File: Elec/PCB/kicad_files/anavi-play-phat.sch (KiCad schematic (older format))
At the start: 8 parts

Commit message: Il faut refaire le pcb avec le port usb de l'autre coté
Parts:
- SW_BCK1, SW_DWN1, SW_L1, SW_OK1, SW_R1, SW_UP1: footprint (none) -> boutton:boutton__5mx5m
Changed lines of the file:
@@
 EESchema Schematic File Version 4
-LIBS:anavi-play-phat-cache
 EELAYER 30 0
 EELAYER END
@@
 F 0 "SW_DWN1" H 7025 3973 50  0000 C CNN
 F 1 "boutton_5mx5m" H 7025 3974 50  0001 C CNN
-F 2 "" H 7150 3700 50  0001 C CNN
+F 2 "boutton:boutton__5mx5m" H 7150 3700 50  0001 C CNN
 F 3 "" H 7150 3700 50  0001 C CNN
 	1    7150 3800
@@
 F 0 "SW_UP1" H 7025 4323 50  0000 C CNN
 F 1 "boutton_5mx5" H 7025 4324 50  0001 C CNN
-F 2 "" H 7150 4050 50  0001 C CNN
+F 2 "boutton:boutton__5mx5m" H 7150 4050 50  0001 C CNN
 F 3 "" H 7150 4050 50  0001 C CNN
 	1    7150 4150
@@
 F 0 "SW_L1" H 7025 4723 50  0000 C CNN
 F 1 "boutton_5mx5m" H 7025 4724 50  0001 C CNN
-F 2 "" H 7150 4450 50  0001 C CNN
+F 2 "boutton:boutton__5mx5m" H 7150 4450 50  0001 C CNN
 F 3 "" H 7150 4450 50  0001 C CNN
 	1    7150 4550
@@
 F 0 "SW_R1" H 7025 5073 50  0000 C CNN
 F 1 "boutton_5mx5m" H 7025 5074 50  0001 C CNN
-F 2 "" H 7150 4800 50  0001 C CNN
+F 2 "boutton:boutton__5mx5m" H 7150 4800 50  0001 C CNN
 F 3 "" H 7150 4800 50  0001 C CNN
 	1    7150 4900
@@
 F 0 "SW_OK1" H 7025 5473 50  0000 C CNN
 F 1 "boutton_5mx5m" H 7025 5474 50  0001 C CNN
-F 2 "" H 7150 5200 50  0001 C CNN
+F 2 "boutton:boutton__5mx5m" H 7150 5200 50  0001 C CNN
 F 3 "" H 7150 5200 50  0001 C CNN
 	1    7150 5300
@@
 F 0 "SW_BCK1" H 7025 5823 50  0000 C CNN
 F 1 "boutton_5mx5m" H 7025 5824 50  0001 C CNN
-F 2 "" H 7150 5550 50  0001 C CNN
+F 2 "boutton:boutton__5mx5m" H 7150 5550 50  0001 C CNN
 F 3 "" H 7150 5550 50  0001 C CNN
 	1    7150 5650

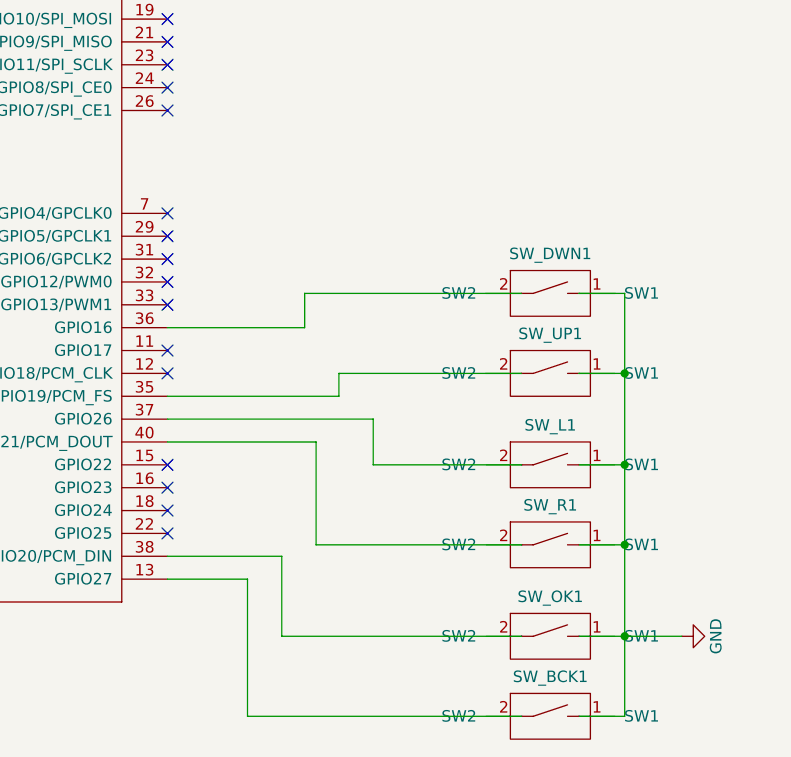
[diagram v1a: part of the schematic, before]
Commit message: PCB v3 correction USB
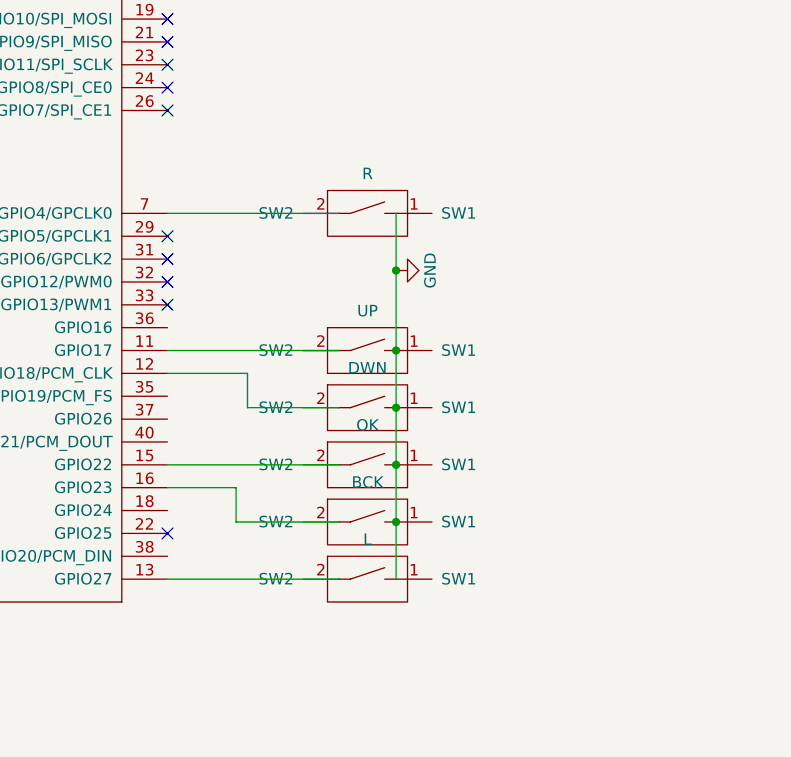
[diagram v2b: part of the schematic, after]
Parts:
- removed SW_BCK1, SW_DWN1, SW_L1, SW_OK1, SW_R1: boutton_5mx5m, boutton:boutton__5mx5m, symbol boutton:boutton_5mx5m
- removed SW_UP1: boutton_5mx5, boutton:boutton__5mx5m, symbol boutton:boutton_5mx5m
- added BCK, DWN, L, OK, R, UP: boutton_6mx6m, boutton:boutton__6mx6m, symbol boutton:boutton_6mx6m
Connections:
- net GND: now also BCK.1 (SW1), DWN.1 (SW1), L.1 (SW1), OK.1 (SW1), R.1 (SW1), UP.1 (SW1)
- net at RASP_CONN1.11 (GPIO17): now also UP.2 (SW2)
- net at RASP_CONN1.12 (GPIO18/PCM_CLK): now also DWN.2 (SW2)
- net at RASP_CONN1.13 (GPIO27): now also L.2 (SW2)
- net at RASP_CONN1.15 (GPIO22): now also OK.2 (SW2)
- net at RASP_CONN1.16 (GPIO23): now also BCK.2 (SW2)
- net at RASP_CONN1.7 (GPIO4/GPCLK0): now also R.2 (SW2)
- no-connect marks 20 -> 14
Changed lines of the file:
@@
 $EndComp
 NoConn ~ 5350 4850
-NoConn ~ 5350 4750
-NoConn ~ 5350 4650
 NoConn ~ 5350 3750
 NoConn ~ 5350 2900
 NoConn ~ 5350 3000
-NoConn ~ 5350 4150
 NoConn ~ 5350 3850
 NoConn ~ 5350 2600
@@
 L anavi-play-phat-rescue:GND-power #PWR016
 U 1 1 5B2D1552
-P 7600 5300
-F 0 "#PWR016" H 7600 5050 50  0001 C CNN
-F 1 "GND" H 7600 5150 50  0000 C CNN
-F 2 "" H 7600 5300 50  0001 C CNN
-F 3 "" H 7600 5300 50  0001 C CNN
-	1    7600 5300
+P 6350 3700
+F 0 "#PWR016" H 6350 3450 50  0001 C CNN
+F 1 "GND" H 6350 3550 50  0000 C CNN
+F 2 "" H 6350 3700 50  0001 C CNN
+F 3 "" H 6350 3700 50  0001 C CNN
+	1    6350 3700
 	0    -1   -1   0
 $EndComp
@@
 	1    0    0    -1
 $EndComp
-Wire Wire Line
-	5350 3950 5950 3950
-Wire Wire Line
-	5950 3950 5950 3800
-Wire Wire Line
-	5950 3800 6900 3800
-Wire Wire Line
-	5350 4250 6100 4250
-Wire Wire Line
-	6100 4250 6100 4150
-Wire Wire Line
-	6100 4150 6900 4150
-Wire Wire Line
-	5350 4950 5850 4950
-Wire Wire Line
-	5850 4950 5850 5300
-Wire Wire Line
-	5850 5300 6900 5300
-Wire Wire Line
-	5350 4350 6250 4350
-Wire Wire Line
-	6250 4350 6250 4550
-Wire Wire Line
-	6250 4550 6900 4550
-Wire Wire Line
-	5350 4450 6000 4450
-Wire Wire Line
-	6000 4450 6000 4900
-Wire Wire Line
-	6000 4900 6900 4900
-Wire Wire Line
-	7150 3800 7350 3800
-Wire Wire Line
-	7350 3800 7350 4150
-Wire Wire Line
-	7350 5300 7600 5300
-Wire Wire Line
-	7150 5300 7350 5300
-Connection ~ 7350 5300
-Wire Wire Line
-	7150 4900 7350 4900
-Connection ~ 7350 4900
-Wire Wire Line
-	7350 4900 7350 5300
-Wire Wire Line
-	7150 4550 7350 4550
-Connection ~ 7350 4550
-Wire Wire Line
-	7350 4550 7350 4900
-Wire Wire Line
-	7150 4150 7350 4150
-Connection ~ 7350 4150
-Wire Wire Line
-	7350 4150 7350 4550
-NoConn ~ 5350 4050
-NoConn ~ 5350 4550
-NoConn ~ 5350 3450
 NoConn ~ 5350 3550
 NoConn ~ 5350 3650
@@
 NoConn ~ 3450 3800
 Wire Wire Line
-	7150 5650 7350 5650
-Wire Wire Line
-	7350 5650 7350 5300
-Wire Wire Line
-	5350 5050 5700 5050
-Wire Wire Line
-	5700 5050 5700 5650
-Wire Wire Line
-	5700 5650 6900 5650
-$Comp
-L boutton:boutton_5mx5m SW_DWN1
-U 1 1 5DD1EB2C
-P 7150 3800
-F 0 "SW_DWN1" H 7025 3973 50  0000 C CNN
-F 1 "boutton_5mx5m" H 7025 3974 50  0001 C CNN
-F 2 "boutton:boutton__5mx5m" H 7150 3700 50  0001 C CNN
-F 3 "" H 7150 3700 50  0001 C CNN
-	1    7150 3800
-	1    0    0    -1
-$EndComp
-$Comp
-L boutton:boutton_5mx5m SW_UP1
-U 1 1 5DD1F4E0
-P 7150 4150
-F 0 "SW_UP1" H 7025 4323 50  0000 C CNN
-F 1 "boutton_5mx5" H 7025 4324 50  0001 C CNN
-F 2 "boutton:boutton__5mx5m" H 7150 4050 50  0001 C CNN
-F 3 "" H 7150 4050 50  0001 C CNN
-	1    7150 4150
-	1    0    0    -1
-$EndComp
-$Comp
-L boutton:boutton_5mx5m SW_L1
-U 1 1 5DD1FF57
-P 7150 4550
-F 0 "SW_L1" H 7025 4723 50  0000 C CNN
-F 1 "boutton_5mx5m" H 7025 4724 50  0001 C CNN
-F 2 "boutton:boutton__5mx5m" H 7150 4450 50  0001 C CNN
-F 3 "" H 7150 4450 50  0001 C CNN
-	1    7150 4550
-	1    0    0    -1
-$EndComp
-$Comp
-L boutton:boutton_5mx5m SW_R1
-U 1 1 5DD20A89
-P 7150 4900
-F 0 "SW_R1" H 7025 5073 50  0000 C CNN
-F 1 "boutton_5mx5m" H 7025 5074 50  0001 C CNN
-F 2 "boutton:boutton__5mx5m" H 7150 4800 50  0001 C CNN
-F 3 "" H 7150 4800 50  0001 C CNN
-	1    7150 4900
-	1    0    0    -1
-$EndComp
-$Comp
-L boutton:boutton_5mx5m SW_OK1
-U 1 1 5DD212C2
-P 7150 5300
-F 0 "SW_OK1" H 7025 5473 50  0000 C CNN
-F 1 "boutton_5mx5m" H 7025 5474 50  0001 C CNN
-F 2 "boutton:boutton__5mx5m" H 7150 5200 50  0001 C CNN
-F 3 "" H 7150 5200 50  0001 C CNN
-	1    7150 5300
-	1    0    0    -1
-$EndComp
-$Comp
-L boutton:boutton_5mx5m SW_BCK1
-U 1 1 5DD21E0C
-P 7150 5650
-F 0 "SW_BCK1" H 7025 5823 50  0000 C CNN
-F 1 "boutton_5mx5m" H 7025 5824 50  0001 C CNN
-F 2 "boutton:boutton__5mx5m" H 7150 5550 50  0001 C CNN
-F 3 "" H 7150 5550 50  0001 C CNN
-	1    7150 5650
-	1    0    0    -1
-$EndComp
+	6350 3450 6350 3700
+$Comp
+L boutton:boutton_6mx6m UP
+U 1 1 5DE76847
+P 6350 4050
+F 0 "UP" H 6225 4223 50  0000 C CNN
+F 1 "boutton_6mx6m" H 6200 3900 50  0001 C CNN
+F 2 "boutton:boutton__6mx6m" H 6350 3950 50  0001 C CNN
+F 3 "" H 6350 3950 50  0001 C CNN
+	1    6350 4050
+	1    0    0    -1
+$EndComp
+$Comp
+L boutton:boutton_6mx6m L
+U 1 1 5DE77762
+P 6350 5050
+F 0 "L" H 6225 5223 50  0000 C CNN
+F 1 "boutton_6mx6m" H 6200 4900 50  0001 C CNN
+F 2 "boutton:boutton__6mx6m" H 6350 4950 50  0001 C CNN
+F 3 "" H 6350 4950 50  0001 C CNN
+	1    6350 5050
+	1    0    0    -1
+$EndComp
+$Comp
+L boutton:boutton_6mx6m OK
+U 1 1 5DE79BAE
+P 6350 4550
+F 0 "OK" H 6225 4723 50  0000 C CNN
+F 1 "boutton_6mx6m" H 6200 4400 50  0001 C CNN
+F 2 "boutton:boutton__6mx6m" H 6350 4450 50  0001 C CNN
+F 3 "" H 6350 4450 50  0001 C CNN
+	1    6350 4550
+	1    0    0    -1
+$EndComp
+$Comp
+L boutton:boutton_6mx6m R
+U 1 1 5DE7B850
+P 6350 3450
+F 0 "R" H 6225 3623 50  0000 C CNN
+F 1 "boutton_6mx6m" H 6200 3300 50  0001 C CNN
+F 2 "boutton:boutton__6mx6m" H 6350 3350 50  0001 C CNN
+F 3 "" H 6350 3350 50  0001 C CNN
+	1    6350 3450
+	1    0    0    -1
+$EndComp
+$Comp
+L boutton:boutton_6mx6m DWN
+U 1 1 5DE7C4F2
+P 6350 4300
+F 0 "DWN" H 6225 4473 50  0000 C CNN
+F 1 "boutton_6mx6m" H 6200 4150 50  0001 C CNN
+F 2 "boutton:boutton__6mx6m" H 6350 4200 50  0001 C CNN
+F 3 "" H 6350 4200 50  0001 C CNN
+	1    6350 4300
+	1    0    0    -1
+$EndComp
+$Comp
+L boutton:boutton_6mx6m BCK
+U 1 1 5DE7DEC3
+P 6350 4800
+F 0 "BCK" H 6225 4973 50  0000 C CNN
+F 1 "boutton_6mx6m" H 6200 4650 50  0001 C CNN
+F 2 "boutton:boutton__6mx6m" H 6350 4700 50  0001 C CNN
+F 3 "" H 6350 4700 50  0001 C CNN
+	1    6350 4800
+	1    0    0    -1
+$EndComp
+Wire Wire Line
+	5350 3450 6100 3450
+Wire Wire Line
+	5350 4050 6100 4050
+Wire Wire Line
+	5350 4150 5700 4150
+Wire Wire Line
+	5700 4150 5700 4300
+Wire Wire Line
+	5700 4300 6100 4300
+Wire Wire Line
+	5350 4550 6100 4550
+Wire Wire Line
+	5350 4650 5650 4650
+Wire Wire Line
+	5650 4650 5650 4800
+Wire Wire Line
+	5650 4800 6100 4800
+Wire Wire Line
+	5350 5050 6100 5050
+Connection ~ 6350 4050
+Wire Wire Line
+	6350 4050 6350 4300
+Connection ~ 6350 4300
+Wire Wire Line
+	6350 4300 6350 4550
+Connection ~ 6350 4550
+Wire Wire Line
+	6350 4550 6350 4800
+Connection ~ 6350 4800
+Wire Wire Line
+	6350 4800 6350 5050
+Connection ~ 6350 3700
+Wire Wire Line
+	6350 3700 6350 4050
 $EndSCHEMATC

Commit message: j'avais pas save déso
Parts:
- renumbered BCK to BCK1, DWN to DWN1, L to L1, OK to OK1, R to R1, UP to UP1
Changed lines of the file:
@@
 	6350 3450 6350 3700
 $Comp
-L boutton:boutton_6mx6m UP
+L boutton:boutton_6mx6m UP1
 U 1 1 5DE76847
 P 6350 4050
-F 0 "UP" H 6225 4223 50  0000 C CNN
+F 0 "UP1" H 6225 4223 50  0000 C CNN
 F 1 "boutton_6mx6m" H 6200 3900 50  0001 C CNN
 F 2 "boutton:boutton__6mx6m" H 6350 3950 50  0001 C CNN
@@
 $EndComp
 $Comp
-L boutton:boutton_6mx6m L
+L boutton:boutton_6mx6m L1
 U 1 1 5DE77762
 P 6350 5050
-F 0 "L" H 6225 5223 50  0000 C CNN
+F 0 "L1" H 6225 5223 50  0000 C CNN
 F 1 "boutton_6mx6m" H 6200 4900 50  0001 C CNN
 F 2 "boutton:boutton__6mx6m" H 6350 4950 50  0001 C CNN
@@
 $EndComp
 $Comp
-L boutton:boutton_6mx6m OK
+L boutton:boutton_6mx6m OK1
 U 1 1 5DE79BAE
 P 6350 4550
-F 0 "OK" H 6225 4723 50  0000 C CNN
+F 0 "OK1" H 6225 4723 50  0000 C CNN
 F 1 "boutton_6mx6m" H 6200 4400 50  0001 C CNN
 F 2 "boutton:boutton__6mx6m" H 6350 4450 50  0001 C CNN
@@
 $EndComp
 $Comp
-L boutton:boutton_6mx6m R
+L boutton:boutton_6mx6m R1
 U 1 1 5DE7B850
 P 6350 3450
-F 0 "R" H 6225 3623 50  0000 C CNN
+F 0 "R1" H 6225 3623 50  0000 C CNN
 F 1 "boutton_6mx6m" H 6200 3300 50  0001 C CNN
 F 2 "boutton:boutton__6mx6m" H 6350 3350 50  0001 C CNN
@@
 $EndComp
 $Comp
-L boutton:boutton_6mx6m DWN
+L boutton:boutton_6mx6m DWN1
 U 1 1 5DE7C4F2
 P 6350 4300
-F 0 "DWN" H 6225 4473 50  0000 C CNN
+F 0 "DWN1" H 6225 4473 50  0000 C CNN
 F 1 "boutton_6mx6m" H 6200 4150 50  0001 C CNN
 F 2 "boutton:boutton__6mx6m" H 6350 4200 50  0001 C CNN
@@
 $EndComp
 $Comp
-L boutton:boutton_6mx6m BCK
+L boutton:boutton_6mx6m BCK1
 U 1 1 5DE7DEC3
 P 6350 4800
-F 0 "BCK" H 6225 4973 50  0000 C CNN
+F 0 "BCK1" H 6225 4973 50  0000 C CNN
 F 1 "boutton_6mx6m" H 6200 4650 50  0001 C CNN
 F 2 "boutton:boutton__6mx6m" H 6350 4700 50  0001 C CNN

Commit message: Le joli pcb
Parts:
- added J1: USB Data, w_conn_misc:header 2m spaced, symbol w_connectors:HEADER_2
- added J2: USB power, w_conn_misc:header 2m spaced, symbol w_connectors:HEADER_2
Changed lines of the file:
@@
 Wire Wire Line
 	6350 3700 6350 4050
+$Comp
+L w_connectors:HEADER_2 J1
+U 1 1 5DF274FA
+P 8450 2650
+F 0 "J1" H 8578 2756 60  0000 L CNN
+F 1 "USB Data" H 8578 2650 60  0000 L CNN
+F 2 "w_conn_misc:header 2m spaced" H 8578 2544 60  0000 L CNN
+F 3 "" H 8450 2650 60  0000 C CNN
+	1    8450 2650
+	1    0    0    -1
+$EndComp
+$Comp
+L w_connectors:HEADER_2 J2
+U 1 1 5DF290D8
+P 8450 3000
+F 0 "J2" H 8578 3106 60  0000 L CNN
+F 1 "USB power" H 8578 3000 60  0000 L CNN
+F 2 "w_conn_misc:header 2m spaced" H 8578 2894 60  0000 L CNN
+F 3 "" H 8450 3000 60  0000 C CNN
+	1    8450 3000
+	1    0    0    -1
+$EndComp
 $EndSCHEMATC

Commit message: Tout plein de modifs
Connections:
- net +5V: now also J2.1
- net GND: now also J2.2
- net D+: now reaches J1.1
- net D-: now reaches J1.2
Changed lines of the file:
@@
 	1    0    0    -1
 $EndComp
+Wire Wire Line
+	8350 2600 8150 2600
+Wire Wire Line
+	8350 2700 8150 2700
+Wire Wire Line
+	8350 2950 8150 2950
+Wire Wire Line
+	8350 3050 8150 3050
+$Comp
+L anavi-play-phat-rescue:GND-power #PWR?
+U 1 1 5DFB5C7E
+P 8150 3050
+F 0 "#PWR?" H 8150 2800 50  0001 C CNN
+F 1 "GND-power" H 8155 2877 50  0000 C CNN
+F 2 "" H 8150 3050 50  0001 C CNN
+F 3 "" H 8150 3050 50  0001 C CNN
+	1    8150 3050
+	1    0    0    -1
+$EndComp
+$Comp
+L anavi-play-phat-rescue:+5V-power #PWR?
+U 1 1 5DFB7142
+P 8150 2950
+F 0 "#PWR?" H 8150 2800 50  0001 C CNN
+F 1 "+5V-power" V 8165 3077 50  0000 L CNN
+F 2 "" H 8150 2950 50  0001 C CNN
+F 3 "" H 8150 2950 50  0001 C CNN
+	1    8150 2950
+	0    -1   -1   0
+$EndComp
+Text GLabel 8150 2600 0    50   Input ~ 0
+D+
+Text GLabel 8150 2700 0    50   Input ~ 0
+D-
 $EndSCHEMATC
